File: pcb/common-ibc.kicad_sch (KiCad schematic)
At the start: 112 parts, among them J1 XILINX_JTAG, J10 U.FL, J11 MOLEX_0039291087, J2 MOLEX_0039291067, J3 GROUND, J4 GROUND, J5 MOLEX_0532610571, J6 U.FL, J7 U.FL, J8 U.FL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

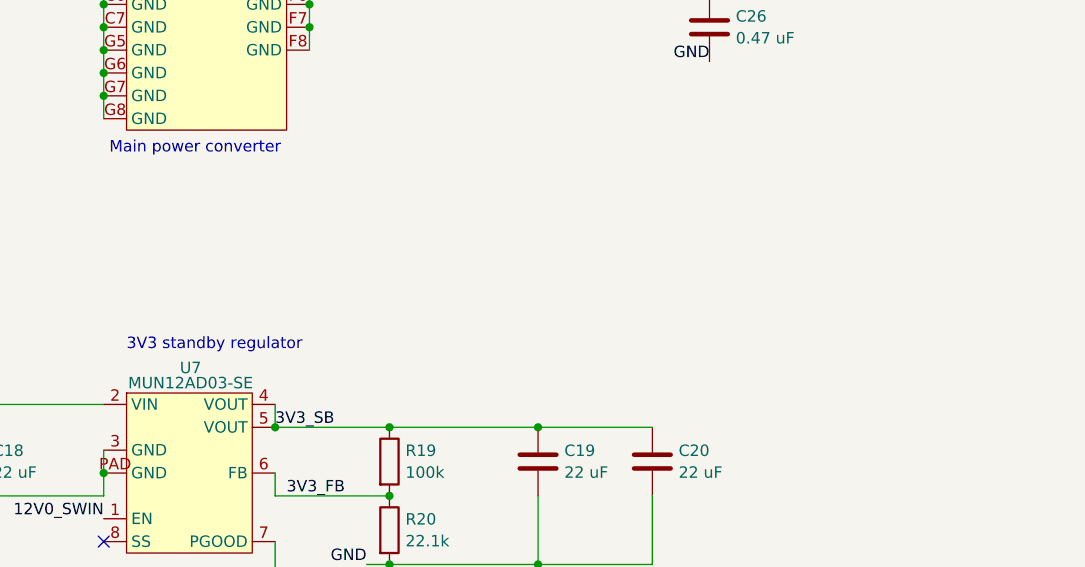
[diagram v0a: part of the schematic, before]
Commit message: Initial refactoring to task model
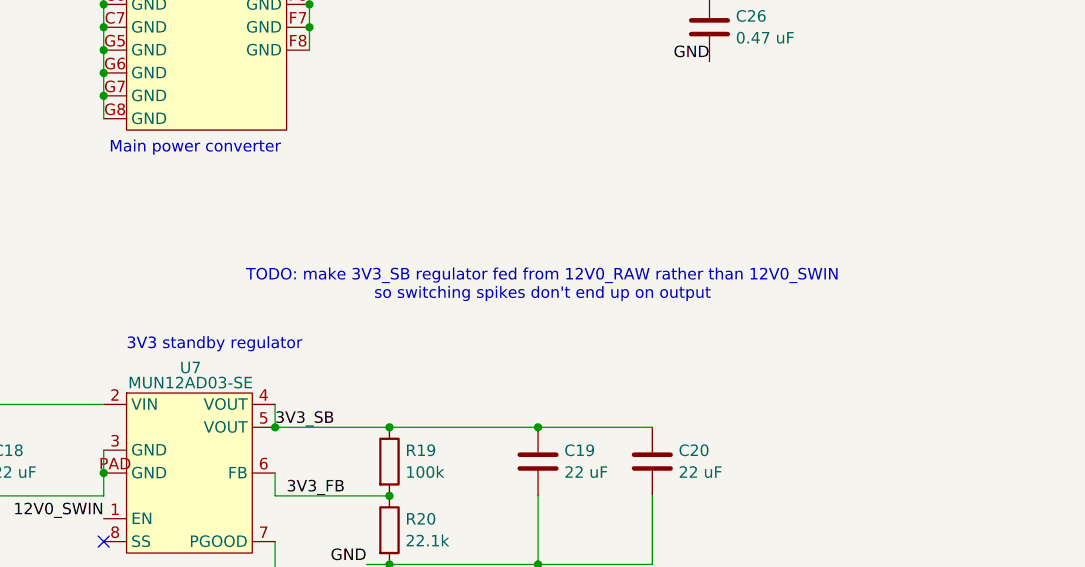
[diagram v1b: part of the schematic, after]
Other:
- note added: "TODO: make 3V3_SB regulator fed from 12V0_RAW rather than 12V0_SWIN so switching spikes don't end up on output"
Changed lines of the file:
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@@
+		)
+	)
+	(text "TODO: make 3V3_SB regulator fed from 12V0_RAW rather than 12V0_SWIN \nso switching spikes don't end up on output"
+		(exclude_from_sim no)
+		(at 250.698 226.822 0)
+		(effects
+			(font
+				(size 1.27 1.27)
+			)
 		)
 	)
